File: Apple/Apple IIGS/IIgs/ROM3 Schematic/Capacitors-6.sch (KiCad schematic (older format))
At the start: 98 parts

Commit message: Clean-up after detailed circuit analysis - Fixed Reference to library in project file - Fixed BABUS tags on HCT245 (had wrong nets) - Flipped HCT245 circuits on MEGAII page to better match In/Out flow - Changed HCT245 symbol to move enable and DIR to better match In/Out Flow - Changed HCT245 into multi-unit symbol to put VCC/GND pins on Unit B - Fixed MEGAII designator - Fixed ADBUS nets on HCT245 (should be ABUS!) - Added notes with lessons learned from circuit deep-dive
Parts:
- JP24: symbol IIgs-Schematic-rescue:M02-freetronics_schematic -> IIgs-Schematic-rescue:M02-freetronics_schematic-IIgs-Schematic-rescue
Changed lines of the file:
@@
 $EndComp
 $Comp
-L IIgs-Schematic-rescue:M02-freetronics_schematic JP24
+L IIgs-Schematic-rescue:M02-freetronics_schematic-IIgs-Schematic-rescue JP24
 U 1 1 5E2DFE04
 P 8450 5850

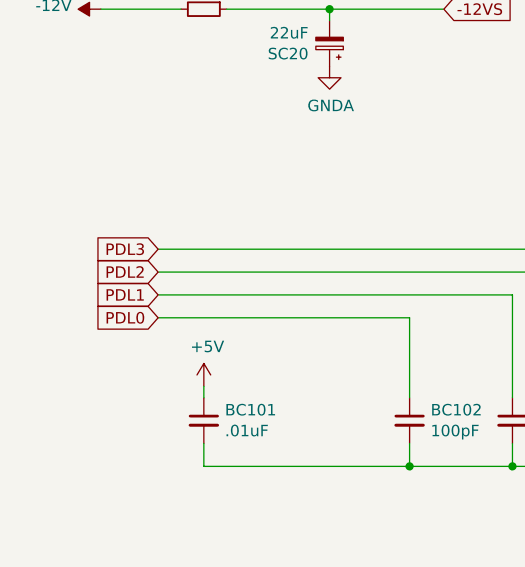
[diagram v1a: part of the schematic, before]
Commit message: started v2 updates on iigs-rom3
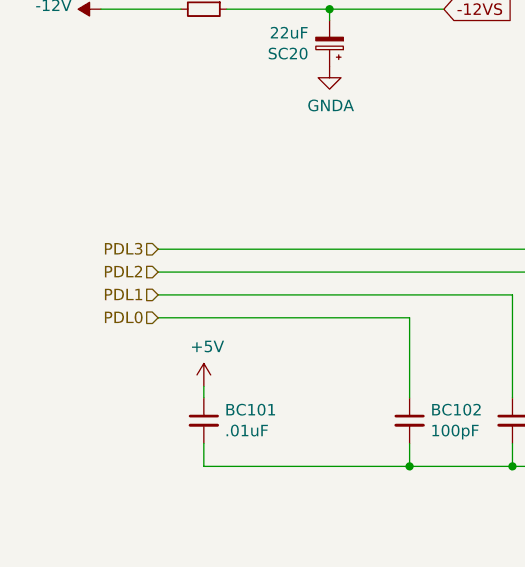
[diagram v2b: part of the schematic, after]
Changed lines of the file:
@@
 $Descr A4 11693 8268
 encoding utf-8
-Sheet 7 10
+Sheet 6 10
 Title ""
 Date ""
-Rev ""
+Rev "2"
 Comp ""
 Comment1 ""
@@
 Text GLabel 2350 4400 2    50   Input ~ 0
 -5VS
-Text GLabel 2350 5200 2    50   Input ~ 0
--12VS
 Text GLabel 4350 3800 3    50   Input ~ 0
 -12VS
 Text Notes 7200 6700 0    50   ~ 0
 Investigate with the "-5VS" and "-12VS" nodes are doing
-Text GLabel 1100 6250 0    50   Input ~ 0
-PDL3
-Text GLabel 1100 6350 0    50   Input ~ 0
-PDL2
-Text GLabel 1100 6450 0    50   Input ~ 0
-PDL1
-Text GLabel 1100 6550 0    50   Input ~ 0
-PDL0
 $Comp
 L Device:C_Small BC101
@@
 	3200 4900 3200 4850
 Connection ~ 3200 4850
+Text HLabel 1100 6250 0    50   Input ~ 0
+PDL3
+Text HLabel 1100 6350 0    50   Input ~ 0
+PDL2
+Text HLabel 1100 6450 0    50   Input ~ 0
+PDL1
+Text HLabel 1100 6550 0    50   Input ~ 0
+PDL0
+Text GLabel 2350 5200 2    50   Input ~ 0
+-12VS
 $EndSCHEMATC
